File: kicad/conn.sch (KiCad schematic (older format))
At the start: 3 parts, among them J1701 NHD-4.3-480272FT-CTXL-T, J1702 NHD-4.3-480272FT-CTXL-T, J1703 NHD-4.3-480272FT-CTXL-T

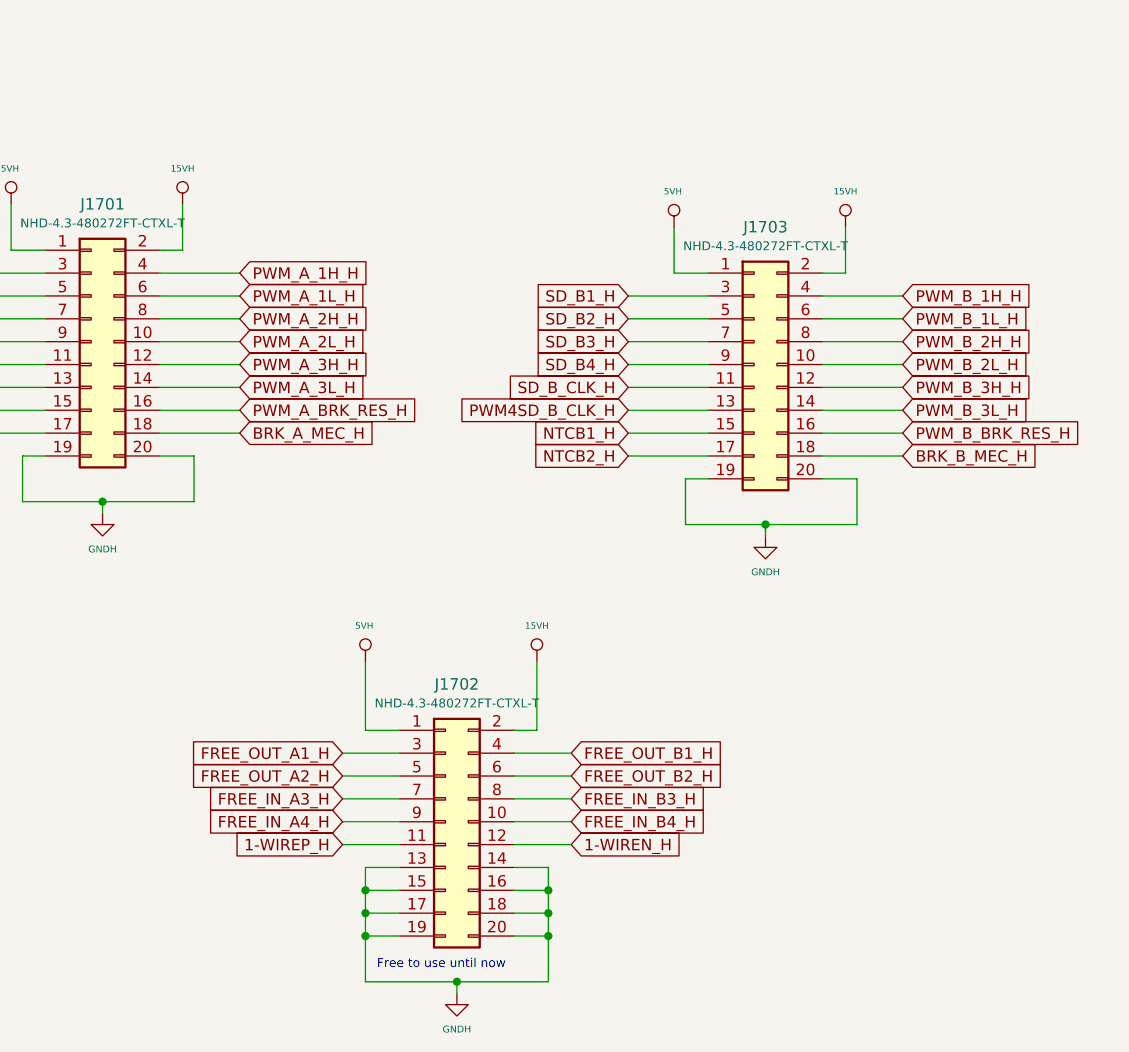
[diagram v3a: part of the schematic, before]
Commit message: I forgot that QUEP was diferential!! all to back....
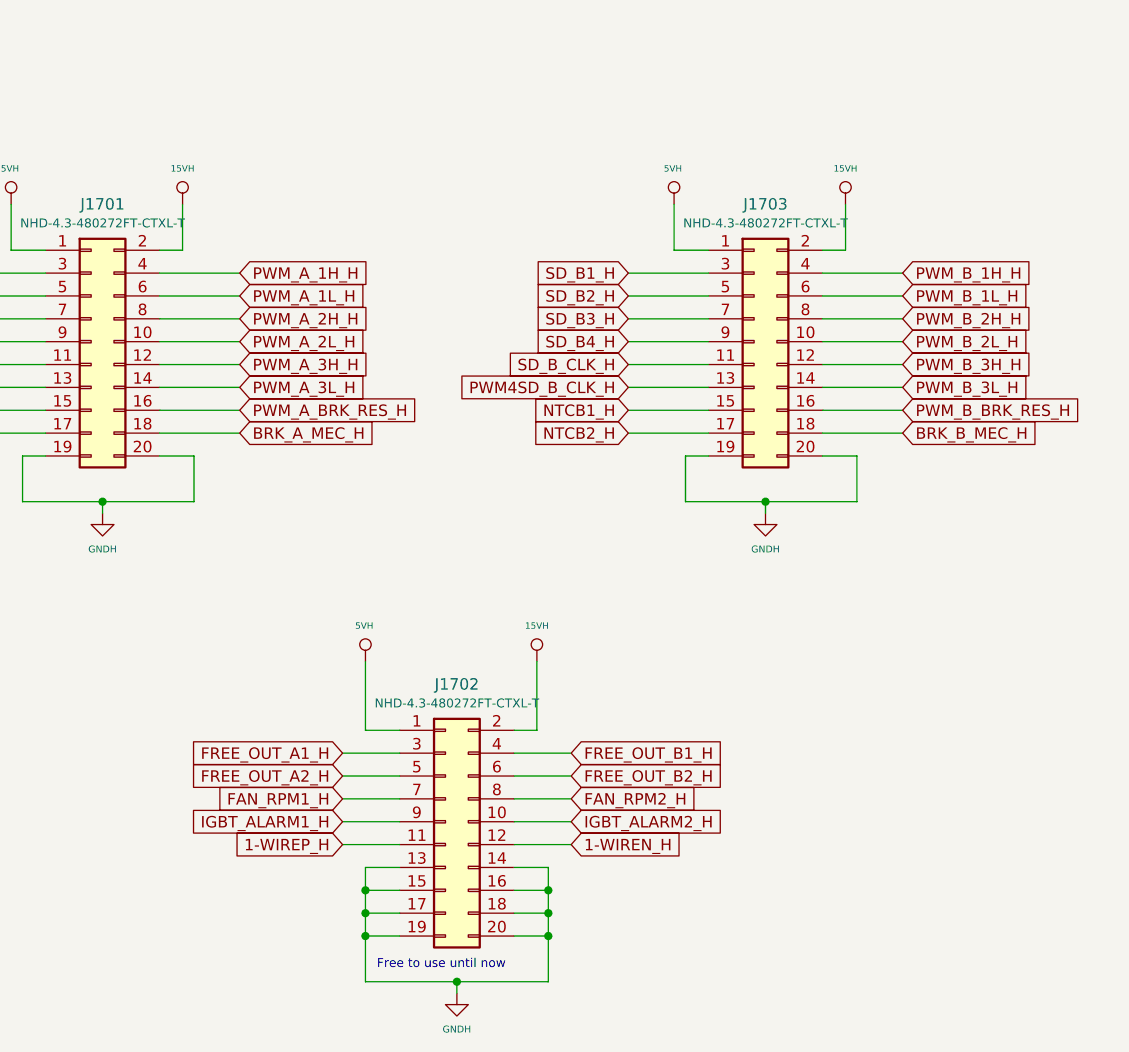
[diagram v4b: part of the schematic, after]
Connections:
- net FREE_IN_A3_H renamed FAN_RPM1_H
- net FREE_IN_A4_H renamed IGBT_ALARM1_H
- net FREE_IN_B3_H renamed FAN_RPM2_H
- net FREE_IN_B4_H renamed IGBT_ALARM2_H
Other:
- moved on the sheet: J1703
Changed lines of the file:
@@
 $Descr A3 16535 11693
 encoding utf-8
-Sheet 17 18
+Sheet 17 19
 Title "Common connections"
 Date "2020-01-09"
@@
 Common Connections
 Wire Wire Line
-	10300 2650 9950 2650
-Wire Wire Line
-	9950 2750 10300 2750
-Wire Wire Line
-	10300 2850 9950 2850
-Wire Wire Line
-	9950 2950 10300 2950
+	10300 2550 9950 2550
+Wire Wire Line
+	9950 2650 10300 2650
+Wire Wire Line
+	10300 2750 9950 2750
+Wire Wire Line
+	9950 2850 10300 2850
+Wire Wire Line
+	10300 2950 9950 2950
+Wire Wire Line
+	10300 3150 9950 3150
 Wire Wire Line
 	10300 3050 9950 3050
 Wire Wire Line
-	10300 3250 9950 3250
-Wire Wire Line
-	10300 3150 9950 3150
-Wire Wire Line
-	9950 2550 10300 2550
-Wire Wire Line
-	9950 3350 10100 3350
-Wire Wire Line
-	9450 2750 9100 2750
-Wire Wire Line
-	9100 2850 9450 2850
-Wire Wire Line
-	9450 2950 9100 2950
+	9950 2450 10300 2450
+Wire Wire Line
+	9950 3250 10100 3250
+Wire Wire Line
+	9450 2650 9100 2650
+Wire Wire Line
+	9100 2750 9450 2750
+Wire Wire Line
+	9450 2850 9100 2850
+Wire Wire Line
+	9100 2950 9450 2950
 Wire Wire Line
 	9100 3050 9450 3050
 Wire Wire Line
-	9100 3150 9450 3150
-Wire Wire Line
-	9100 2650 9450 2650
-Wire Wire Line
 	9100 2550 9450 2550
+Wire Wire Line
+	9100 2450 9450 2450
 $Comp
 L servo:GNDH #PWR?
 U 1 1 605AFA1C
-P 9700 3600
+P 9700 3500
 AR Path="/5DDE8C5E/605AFA1C" Ref="#PWR?"  Part="1"
 AR Path="/5EC40F3C/605AFA1C" Ref="#PWR01708"  Part="1"
-F 0 "#PWR01708" H 9700 3350 30  0001 C CNN
-F 1 "GNDH" H 9700 3442 30  0000 C CNN
-F 2 "" H 9700 3600 50  0001 C CNN
-F 3 "" H 9700 3600 50  0001 C CNN
-	1    9700 3600
-	-1   0    0    -1
-$EndComp
-Wire Wire Line
-	9450 3350 9350 3350
+F 0 "#PWR01708" H 9700 3250 30  0001 C CNN
+F 1 "GNDH" H 9700 3342 30  0000 C CNN
+F 2 "" H 9700 3500 50  0001 C CNN
+F 3 "" H 9700 3500 50  0001 C CNN
+	1    9700 3500
+	-1   0    0    -1
+$EndComp
+Wire Wire Line
+	9450 3250 9350 3250
 $Comp
 L servo:5VH #PWR?
 U 1 1 605AFA23
-P 9300 2250
+P 9300 2150
 AR Path="/5DDE8C5E/605AFA23" Ref="#PWR?"  Part="1"
 AR Path="/5EC40F3C/605AFA23" Ref="#PWR01707"  Part="1"
-F 0 "#PWR01707" H 9300 2050 20  0001 C CNN
-F 1 "5VH" H 9305 2407 28  0000 C CNN
-F 2 "" H 9300 2250 50  0001 C CNN
-F 3 "" H 9300 2250 50  0001 C CNN
-	1    9300 2250
-	-1   0    0    -1
-$EndComp
-Wire Wire Line
-	9300 2250 9300 2450
-Wire Wire Line
-	9300 2450 9450 2450
-Wire Wire Line
-	10050 2250 10050 2450
-Wire Wire Line
-	10050 2450 9950 2450
-Wire Wire Line
-	10100 3350 10100 3550
-Wire Wire Line
-	10100 3550 9700 3550
-Wire Wire Line
-	9700 3550 9700 3600
-Wire Wire Line
-	9350 3550 9700 3550
-Connection ~ 9700 3550
-Wire Wire Line
-	9350 3350 9350 3550
+F 0 "#PWR01707" H 9300 1950 20  0001 C CNN
+F 1 "5VH" H 9305 2307 28  0000 C CNN
+F 2 "" H 9300 2150 50  0001 C CNN
+F 3 "" H 9300 2150 50  0001 C CNN
+	1    9300 2150
+	-1   0    0    -1
+$EndComp
+Wire Wire Line
+	9300 2150 9300 2350
+Wire Wire Line
+	9300 2350 9450 2350
+Wire Wire Line
+	10050 2150 10050 2350
+Wire Wire Line
+	10050 2350 9950 2350
+Wire Wire Line
+	10100 3250 10100 3450
+Wire Wire Line
+	10100 3450 9700 3450
+Wire Wire Line
+	9700 3450 9700 3500
+Wire Wire Line
+	9350 3450 9700 3450
+Connection ~ 9700 3450
+Wire Wire Line
+	9350 3250 9350 3450
 Wire Wire Line
 	8600 5350 8750 5350
@@
 Connection ~ 8750 5350
 Wire Wire Line
-	8600 5050 8750 5050
-Wire Wire Line
-	8750 5050 8750 5150
-Wire Wire Line
 	8600 5150 8750 5150
-Connection ~ 8750 5150
 Wire Wire Line
 	8600 5250 8750 5250
@@
 	8750 5250 8750 5350
 Wire Wire Line
-	8100 5050 7950 5050
-Wire Wire Line
-	7950 5050 7950 5150
-Wire Wire Line
 	8100 5150 7950 5150
-Connection ~ 7950 5150
 Wire Wire Line
 	8100 5250 7950 5250
@@
 Text Notes 8000 5500 0    39   ~ 0
 Free to use until now
+Text GLabel 10300 2450 2    50   Input ~ 0
+PWM_B_1H_H
 Text GLabel 10300 2550 2    50   Input ~ 0
-PWM_B_1H_H
+PWM_B_1L_H
 Text GLabel 10300 2650 2    50   Input ~ 0
-PWM_B_1L_H
+PWM_B_2H_H
 Text GLabel 10300 2750 2    50   Input ~ 0
-PWM_B_2H_H
+PWM_B_2L_H
 Text GLabel 10300 2850 2    50   Input ~ 0
-PWM_B_2L_H
+PWM_B_3H_H
 Text GLabel 10300 2950 2    50   Input ~ 0
-PWM_B_3H_H
+PWM_B_3L_H
 Text GLabel 10300 3050 2    50   Input ~ 0
-PWM_B_3L_H
+PWM_B_BRK_RES_H
 Text GLabel 10300 3150 2    50   Input ~ 0
-PWM_B_BRK_RES_H
-Text GLabel 10300 3250 2    50   Input ~ 0
 BRK_B_MEC_H
 Text GLabel 8850 4550 2    50   Input ~ 0
@@
 Text GLabel 8850 4650 2    50   Input ~ 0
 FREE_OUT_B2_H
-Text GLabel 8850 4750 2    50   Input ~ 0
-FREE_IN_B3_H
-Text GLabel 8850 4850 2    50   Input ~ 0
-FREE_IN_B4_H
+Text GLabel 9100 2450 0    50   Input ~ 0
+SD_B1_H
 Text GLabel 9100 2550 0    50   Input ~ 0
-SD_B1_H
+SD_B2_H
 Text GLabel 9100 2650 0    50   Input ~ 0
-SD_B2_H
+SD_B3_H
 Text GLabel 9100 2750 0    50   Input ~ 0
-SD_B3_H
+SD_B4_H
 Text GLabel 9100 2850 0    50   Input ~ 0
-SD_B4_H
+SD_B_CLK_H
 Text GLabel 9100 2950 0    50   Input ~ 0
-SD_B_CLK_H
-Text GLabel 9100 3050 0    50   Input ~ 0
 PWM4SD_B_CLK_H
 Text GLabel 7850 4950 0    50   Input ~ 0
@@
 L servo:15VH #PWR?
 U 1 1 605AFA8F
-P 10050 2250
+P 10050 2150
 AR Path="/5DDE8C5E/605AFA8F" Ref="#PWR?"  Part="1"
 AR Path="/5EC40F3C/605AFA8F" Ref="#PWR01709"  Part="1"
-F 0 "#PWR01709" H 10050 2050 20  0001 C CNN
-F 1 "15VH" H 10050 2407 28  0000 C CNN
-F 2 "" H 10050 2250 50  0001 C CNN
-F 3 "" H 10050 2250 50  0001 C CNN
-	1    10050 2250
+F 0 "#PWR01709" H 10050 1950 20  0001 C CNN
+F 1 "15VH" H 10050 2307 28  0000 C CNN
+F 2 "" H 10050 2150 50  0001 C CNN
+F 3 "" H 10050 2150 50  0001 C CNN
+	1    10050 2150
 	1    0    0    -1
 $EndComp
@@
 Text GLabel 7850 4650 0    50   Input ~ 0
 FREE_OUT_A2_H
-Text GLabel 7850 4750 0    50   Input ~ 0
-FREE_IN_A3_H
-Text GLabel 7850 4850 0    50   Input ~ 0
-FREE_IN_A4_H
 $Comp
 L servo:15VH #PWR?
@@
 Text GLabel 6200 3050 0    50   Input ~ 0
 NTCA1_H
-Text GLabel 9100 3150 0    50   Input ~ 0
+Text GLabel 9100 3050 0    50   Input ~ 0
 NTCB1_H
 Text GLabel 6200 3150 0    50   Input ~ 0
 NTCA2_H
-Text GLabel 9100 3250 0    50   Input ~ 0
+Text GLabel 9100 3150 0    50   Input ~ 0
 NTCB2_H
 Wire Wire Line
 	6200 3150 6550 3150
 Wire Wire Line
-	9100 3250 9450 3250
+	9100 3150 9450 3150
 $Comp
 L servo:NHD-4.3-480272FT-CTXL-T J?
@@
 L servo:NHD-4.3-480272FT-CTXL-T J?
 U 1 1 5E350A93
-P 9650 2850
+P 9650 2750
 AR Path="/5E72D841/5E350A93" Ref="J?"  Part="1"
 AR Path="/5EC40F3C/5E350A93" Ref="J1703"  Part="1"
-F 0 "J1703" H 9700 3451 50  0000 C CNN
-F 1 "NHD-4.3-480272FT-CTXL-T" H 9700 3368 39  0000 C CNN
-F 2 "Connector_IDC:IDC-Header_2x10_P2.54mm_Vertical" H 9650 2850 50  0001 C CNN
-F 3 "../doc/datasheets/NHD-4.3-480272FT-CTXL-T.pdf" H 9700 3350 50  0001 C CNN
-	1    9650 2850
-	1    0    0    -1
-$EndComp
+F 0 "J1703" H 9700 3351 50  0000 C CNN
+F 1 "NHD-4.3-480272FT-CTXL-T" H 9700 3268 39  0000 C CNN
+F 2 "Connector_IDC:IDC-Header_2x10_P2.54mm_Vertical" H 9650 2750 50  0001 C CNN
+F 3 "../doc/datasheets/NHD-4.3-480272FT-CTXL-T.pdf" H 9700 3250 50  0001 C CNN
+	1    9650 2750
+	1    0    0    -1
+$EndComp
+Wire Wire Line
+	8600 5050 8750 5050
+Text GLabel 7850 4750 0    50   Input ~ 0
+FAN_RPM1_H
+Text GLabel 7850 4850 0    50   Input ~ 0
+IGBT_ALARM1_H
+Wire Wire Line
+	8750 5150 8750 5050
+Connection ~ 8750 5150
+Wire Wire Line
+	7950 5150 7950 5050
+Connection ~ 7950 5150
+Wire Wire Line
+	7950 5050 8100 5050
+Text GLabel 8850 4750 2    50   Input ~ 0
+FAN_RPM2_H
+Text GLabel 8850 4850 2    50   Input ~ 0
+IGBT_ALARM2_H
 $EndSCHEMATC

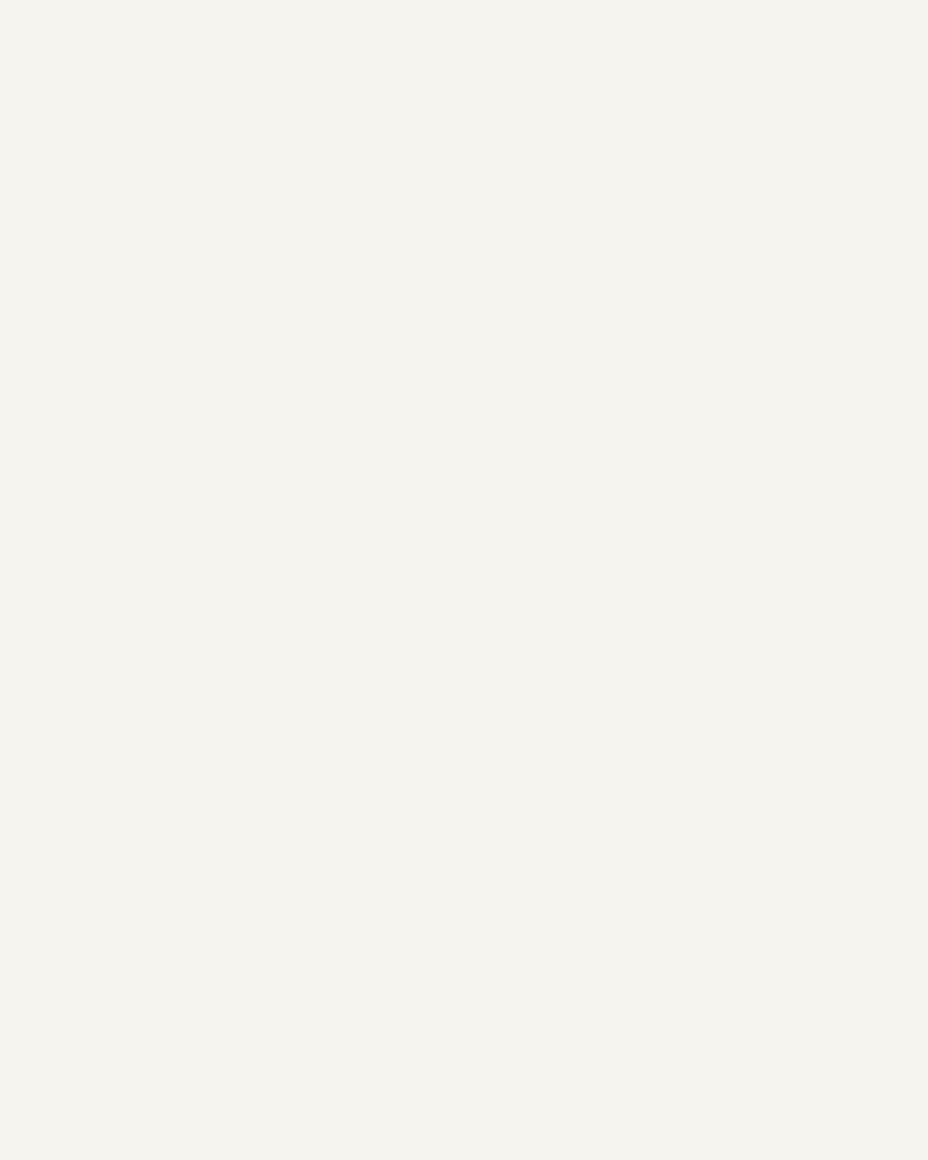
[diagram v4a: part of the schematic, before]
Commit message: mofifing ac/dc position and 3 idc out to 2
I've triung to reacomodate the ac/dc power supplies to manage isolation
and free space using 2 idc instead of 3
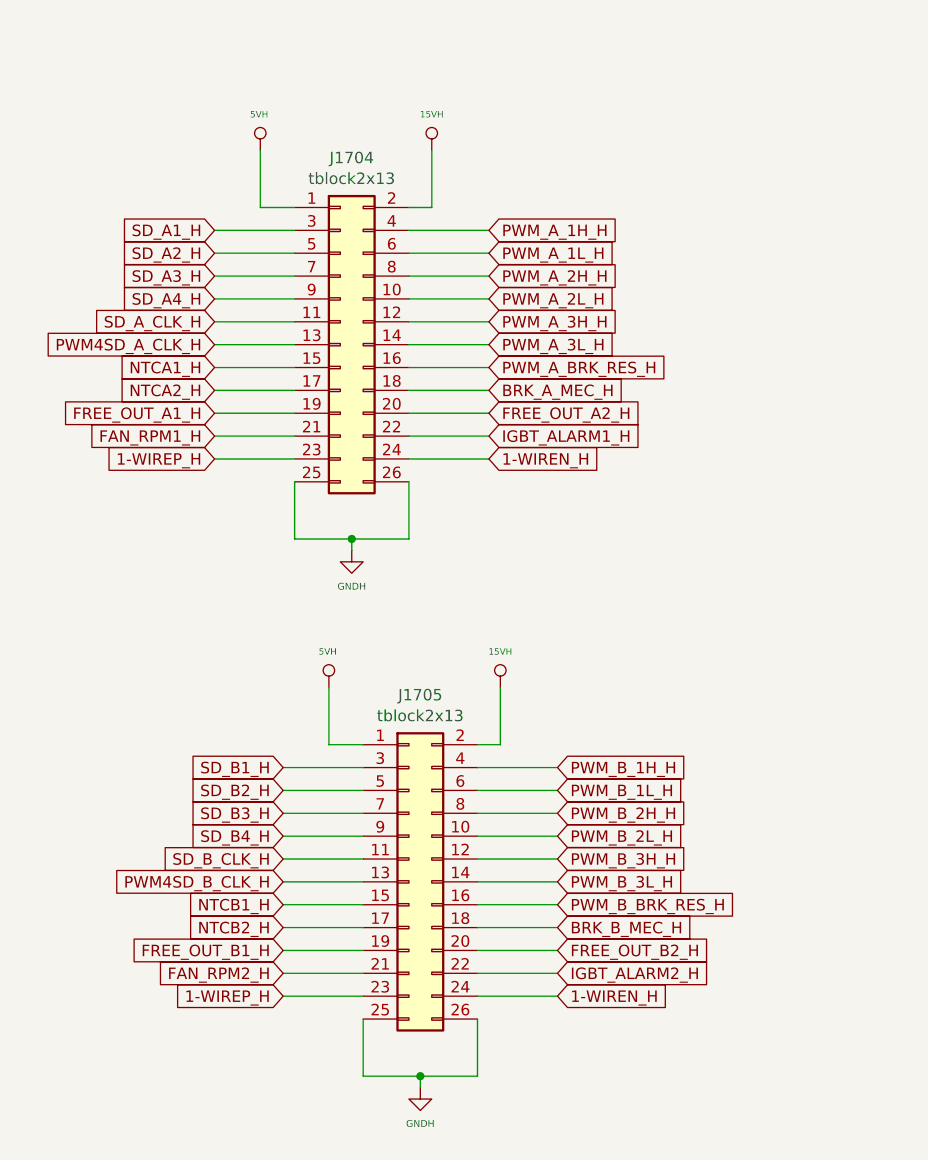
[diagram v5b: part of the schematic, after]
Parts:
- added J1704, J1705: tblock2x13, Connector_IDC:IDC-Header_2x13_P2.54mm_Vertical, symbol Connector_Generic:Conn_02x13_Odd_Even
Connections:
- net 1-WIREN_H: now also J1704.24 (Pin_24), J1705.24 (Pin_24)
- net 1-WIREP_H: now also J1704.23 (Pin_23), J1705.23 (Pin_23)
- net 15VH: now also J1704.2 (Pin_2), J1705.2 (Pin_2)
- net 5VH: now also J1704.1 (Pin_1), J1705.1 (Pin_1)
- net BRK_A_MEC_H: now also J1704.18 (Pin_18)
- net BRK_B_MEC_H: now also J1705.18 (Pin_18)
- net FAN_RPM1_H: now also J1704.21 (Pin_21)
- net FAN_RPM2_H: now also J1705.21 (Pin_21)
- net FREE_OUT_A1_H: now also J1704.19 (Pin_19)
- net FREE_OUT_A2_H: now also J1704.20 (Pin_20)
- net FREE_OUT_B1_H: now also J1705.19 (Pin_19)
- net FREE_OUT_B2_H: now also J1705.20 (Pin_20)
- net GNDH: now also J1704.25 (Pin_25), J1704.26 (Pin_26), J1705.25 (Pin_25), J1705.26 (Pin_26)
- net IGBT_ALARM1_H: now also J1704.22 (Pin_22)
- net IGBT_ALARM2_H: now also J1705.22 (Pin_22)
- net NTCA1_H: now also J1704.15 (Pin_15)
- net NTCA2_H: now also J1704.17 (Pin_17)
- net NTCB1_H: now also J1705.15 (Pin_15)
- net NTCB2_H: now also J1705.17 (Pin_17)
- net PWM4SD_A_CLK_H: now also J1704.13 (Pin_13)
- net PWM4SD_B_CLK_H: now also J1705.13 (Pin_13)
- net PWM_A_1H_H: now also J1704.4 (Pin_4)
- net PWM_A_1L_H: now also J1704.6 (Pin_6)
- net PWM_A_2H_H: now also J1704.8 (Pin_8)
- net PWM_A_2L_H: now also J1704.10 (Pin_10)
- net PWM_A_3H_H: now also J1704.12 (Pin_12)
- net PWM_A_3L_H: now also J1704.14 (Pin_14)
- net PWM_A_BRK_RES_H: now also J1704.16 (Pin_16)
- net PWM_B_1H_H: now also J1705.4 (Pin_4)
- net PWM_B_1L_H: now also J1705.6 (Pin_6)
- net PWM_B_2H_H: now also J1705.8 (Pin_8)
- net PWM_B_2L_H: now also J1705.10 (Pin_10)
- net PWM_B_3H_H: now also J1705.12 (Pin_12)
- net PWM_B_3L_H: now also J1705.14 (Pin_14)
- net PWM_B_BRK_RES_H: now also J1705.16 (Pin_16)
- net SD_A1_H: now also J1704.3 (Pin_3)
- net SD_A2_H: now also J1704.5 (Pin_5)
- net SD_A3_H: now also J1704.7 (Pin_7)
- net SD_A4_H: now also J1704.9 (Pin_9)
- net SD_A_CLK_H: now also J1704.11 (Pin_11)
- net SD_B1_H: now also J1705.3 (Pin_3)
- net SD_B2_H: now also J1705.5 (Pin_5)
- net SD_B3_H: now also J1705.7 (Pin_7)
- net SD_B4_H: now also J1705.9 (Pin_9)
- net SD_B_CLK_H: now also J1705.11 (Pin_11)

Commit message: beginine routing... far far away
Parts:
- removed J1701, J1702, J1703: NHD-4.3-480272FT-CTXL-T, Connector_IDC:IDC-Header_2x10_P2.54mm_Vertical, symbol servo:NHD-4.3-480272FT-CTXL-T
- removed J1704, J1705: tblock2x13, Connector_IDC:IDC-Header_2x13_P2.54mm_Vertical, symbol Connector_Generic:Conn_02x13_Odd_Even
- added J1704, J1705: idc2x17, servo:idc2x17_smd, symbol Connector_Generic:Conn_02x17_Odd_Even
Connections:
- net 15VH: now also J1704.10 (Pin_10), J1704.32 (Pin_32), J1704.34 (Pin_34), J1705.10 (Pin_10), J1705.32 (Pin_32), J1705.34 (Pin_34)
- net 5VH: now also J1704.31 (Pin_31), J1704.33 (Pin_33), J1704.9 (Pin_9), J1705.31 (Pin_31), J1705.33 (Pin_33), J1705.9 (Pin_9)
- net FAN_RPM1_H: now also J1704.8 (Pin_8)
- net FAN_RPM2_H: now also J1705.8 (Pin_8)
- net GNDH: now also J1704.1 (Pin_1), J1704.2 (Pin_2), J1704.23 (Pin_23), J1704.24 (Pin_24), J1704.3 (Pin_3), J1704.4 (Pin_4), J1705.1 (Pin_1), J1705.2 (Pin_2), J1705.23 (Pin_23), J1705.24 (Pin_24), J1705.3 (Pin_3), J1705.4 (Pin_4)
- net IGBT_ALARM1_H: now also J1704.7 (Pin_7)
- net IGBT_ALARM2_H: now also J1705.7 (Pin_7)
- new net 1-WIRE_N_H: J1704.30 (Pin_30), J1705.30 (Pin_30)
- new net 1-WIRE_P_H: J1704.29 (Pin_29), J1705.29 (Pin_29)
- new net BRK_MEC1_H: J1704.25 (Pin_25)
- new net BRK_MEC2_H: J1705.25 (Pin_25)
- new net BRK_RES1_H: J1704.26 (Pin_26)
- new net BRK_RES2_H: J1705.26 (Pin_26)
- new net FREE_OUT1_1_H: J1704.5 (Pin_5)
- new net FREE_OUT1_2_H: J1704.6 (Pin_6)
- new net FREE_OUT2_1_H: J1705.5 (Pin_5)
- new net FREE_OUT2_2_H: J1705.6 (Pin_6)
- new net IGBT1_UH_H: J1704.12 (Pin_12)
- new net IGBT1_UL_H: J1704.14 (Pin_14)
- new net IGBT1_VH_H: J1704.16 (Pin_16)
- new net IGBT1_VL_H: J1704.18 (Pin_18)
- new net IGBT1_WH_H: J1704.20 (Pin_20)
- new net IGBT1_WL_H: J1704.22 (Pin_22)
- new net IGBT2_UH_H: J1705.12 (Pin_12)
- new net IGBT2_UL_H: J1705.14 (Pin_14)
- new net IGBT2_VH_H: J1705.16 (Pin_16)
- new net IGBT2_VL_H: J1705.18 (Pin_18)
- new net IGBT2_WH_H: J1705.20 (Pin_20)
- new net IGBT2_WL_H: J1705.22 (Pin_22)
- new net NTC1_1_H: J1704.27 (Pin_27)
- new net NTC1_2_H: J1704.28 (Pin_28)
- new net NTC2_1_H: J1705.27 (Pin_27)
- new net NTC2_2_H: J1705.28 (Pin_28)
- new net SD1_A_H: J1704.17 (Pin_17)
- new net SD1_U_H: J1704.11 (Pin_11)
- new net SD1_V_H: J1704.13 (Pin_13)
- new net SD1_W_H: J1704.15 (Pin_15)
- new net SD2_A_H: J1705.17 (Pin_17)
- new net SD2_U_H: J1705.11 (Pin_11)
- new net SD2_V_H: J1705.13 (Pin_13)
- new net SD2_W_H: J1705.15 (Pin_15)
- new net SD_CLK_IN1_H: J1704.19 (Pin_19)
- new net SD_CLK_IN2_H: J1705.19 (Pin_19)
- new net SD_CLK_OUT1_H: J1704.21 (Pin_21)
- new net SD_CLK_OUT2_H: J1705.21 (Pin_21)
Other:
- note removed: "Free to use until now"
